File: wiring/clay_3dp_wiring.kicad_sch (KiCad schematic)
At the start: 1 part, among them J2 R3.CS

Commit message: update, but need to check references on hierchial sheets
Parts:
- removed J2: R3.CS, symbol Connector_Generic:Conn_01x12
- added A1: Arduino_UNO_R3, Module:Arduino_UNO_R3, symbol MCU_Module:Arduino_UNO_R3
- added J7, J8: TrimTrio connector on project box, symbol Connector_Generic:Conn_01x08
- added J9: 8P8C, symbol Connector:8P8C
- added M1: Stepper_Motor_bipolar, symbol Motor:Stepper_Motor_bipolar
- added U1: MotionKing_2L415B, symbol clay_3dp_wiring:MotionKing_2L415B
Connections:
- new net: J8.1 (Pin_1), M1.1, U1.7 (A+)
- new net: J8.2 (Pin_2), M1.2 (-), U1.8 (A-)
- new net: J8.4 (Pin_4), M1.3, U1.9 (B+)
- new net: J8.5 (Pin_5), M1.4, U1.10 (B-)
- new net 24V_plc_integration_shield/24V IN ORANGE: J7.1 (Pin_1)
- new net 24V_plc_integration_shield/Arduino D2: A1.17 (D2)
- new net 24V_plc_integration_shield/Arduino D4: A1.19 (D4)
- new net 24V_plc_integration_shield/Arduino D7: A1.22 (D7)
- new net 24V_plc_integration_shield/Arduino D8: A1.23 (D8)
- new net 24V_plc_integration_shield/Arduino D9: A1.24 (D9)
- new net 24V_plc_integration_shield/Arduino GND: A1.29 (GND), A1.6 (GND), A1.7 (GND)
- new net 24V_plc_integration_shield/Arduino VIN: A1.8 (VIN)
- new net 24V_plc_integration_shield/Direction signal BLUE: J7.6 (Pin_6)
- new net 24V_plc_integration_shield/GND IN BLACK: J7.3 (Pin_3)
- new net 24V_plc_integration_shield/Motor driver 24V GREY: U1.6 (+V)
- new net 24V_plc_integration_shield/Motor driver 5V PURPLE: U1.3 (OPTO)
- new net 24V_plc_integration_shield/Motor driver DIR WHITE: U1.2 (DIR)
- new net 24V_plc_integration_shield/Motor driver GND YELLOW: U1.5 (GND)
- new net 24V_plc_integration_shield/Motor driver PUL GREEN: U1.1 (PUL)
- new net 24V_plc_integration_shield/Motor driver ~{ENABLE} BROWN: U1.4 (~{ENABLE})
- new net 24V_plc_integration_shield/Run signal RED: J7.5 (Pin_5)
- no-connect marks 0 -> 41
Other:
- added sheet 24V_plc_integration_shield (C:/Users/tetov/src/extruder_ctrl_circuits/24V_plc_integration_shield/24V_plc_integration_shield.kicad_sch)
- added sheet lth2400_robban_io_wiring (lth2400_robban_io_wiring/lth2400_robban_io_wiring.kicad_sch)
- note added: "A+ GREEN (to TrimTrio) GREEN (between 8P8C and stepper)"
- note added: "A- BLACK (to TrimTrio) BLACK (between 8P8C and stepper)"
- note added: "B+ BROWN (to TrimTrio) RED (between 8P8C and stepper)"
- note added: "B- ? (to TrimTrio) ? (between 8P8C and stepper)"
- note added: "Motor driver"
- note added: "TODO: Check which poles on 8P8C are used"

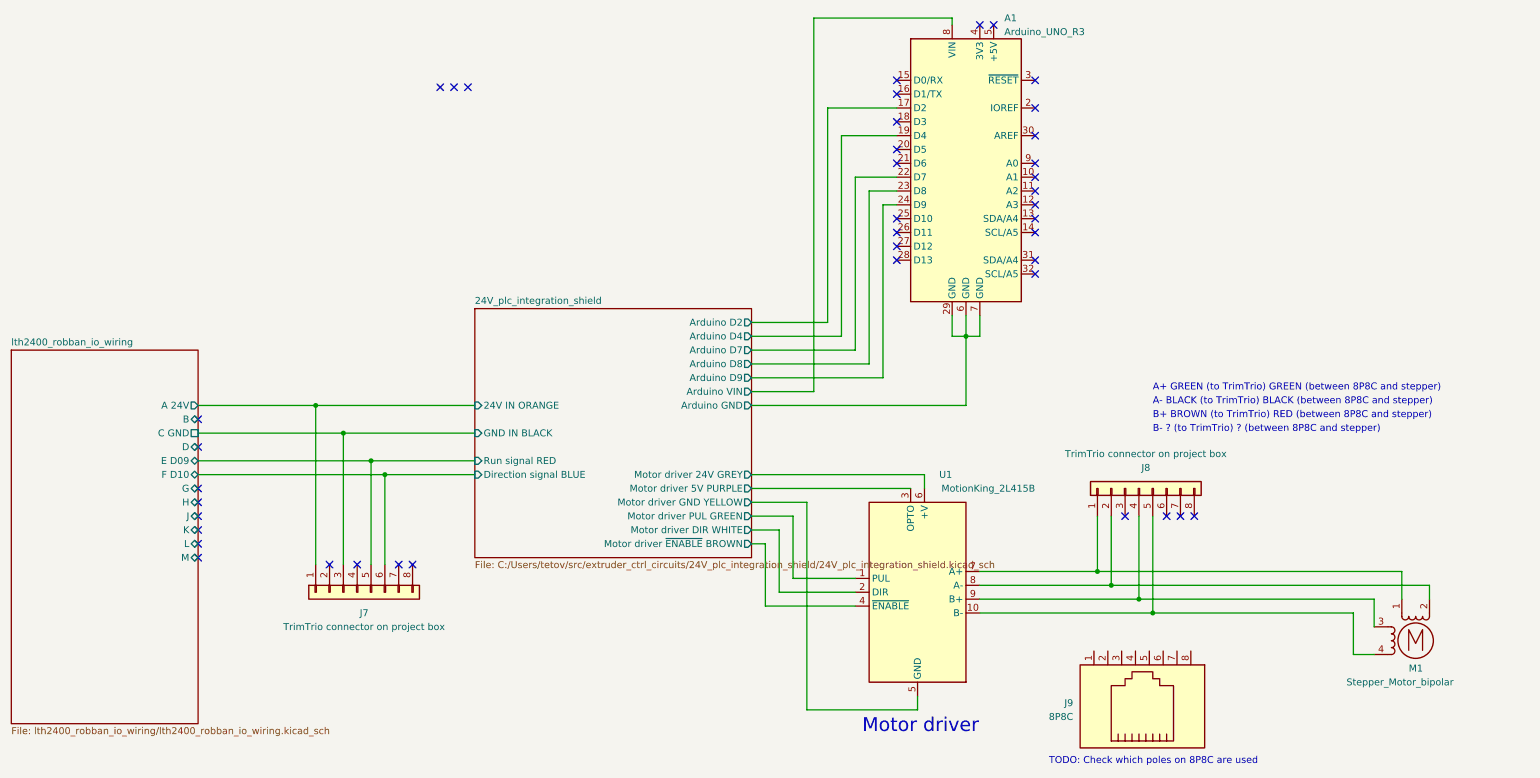
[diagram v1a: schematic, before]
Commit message: documentation of connectors and cable colors
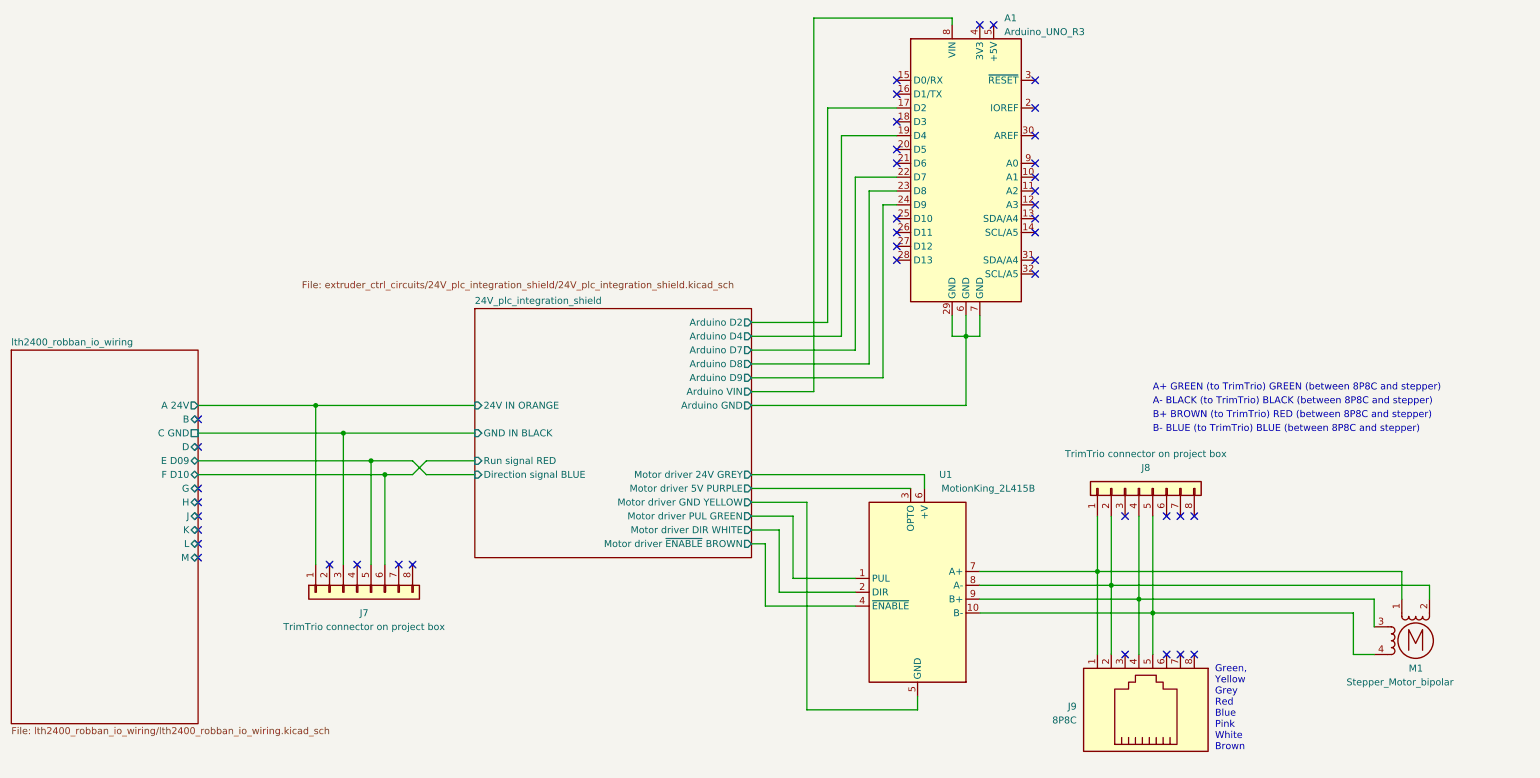
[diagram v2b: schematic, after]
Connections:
- net 24V_plc_integration_shield/Direction signal BLUE: now also J7.5 (Pin_5); no longer J7.6 (Pin_6)
- net 24V_plc_integration_shield/Run signal RED: now also J7.6 (Pin_6); no longer J7.5 (Pin_5)
- net at J9.1: now also J8.1 (Pin_1), M1.1, U1.7 (A+)
- net at J9.2: now also J8.2 (Pin_2), M1.2 (-), U1.8 (A-)
- net at J9.4: now also J8.4 (Pin_4), M1.3, U1.9 (B+)
- net at J9.5: now also J8.5 (Pin_5), M1.4, U1.10 (B-)
- no-connect marks 41 -> 42
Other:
- sheet 24V_plc_integration_shield: file C:/Users/tetov/src/extruder_ctrl_circuits/24V_plc_integration_shield/24V_plc_integration_shield.kicad_sch -> extruder_ctrl_circuits/24V_plc_integration_shield/24V_plc_integration_shield.kicad_sch
- note added: "B- BLUE (to TrimTrio) BLUE (between 8P8C and stepper)"
- note added: "Green, Yellow Grey Red Blue Pink White Brown"
- note removed: "B- ? (to TrimTrio) ? (between 8P8C and stepper)"
- note removed: "Motor driver"
- note removed: "TODO: Check which poles on 8P8C are used"
- moved on the sheet: J9
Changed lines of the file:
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@@
   (junction (at 217.17 118.11) (diameter 0) (color 0 0 0 0)
   )
+  (no_connect (at 232.41 130.81))
   (no_connect (at 193.04 15.24))
   (no_connect (at 49.53 100.33))
+  (no_connect (at 227.33 130.81))
   (no_connect (at 203.2 53.34))
   (no_connect (at 49.53 102.87))
@@
   (no_connect (at 49.53 110.49))
   (no_connect (at 177.8 55.88))
-  (no_connect (at 96.52 26.67))
   (no_connect (at 177.8 58.42))
   (no_connect (at 49.53 107.95))
@@
   (no_connect (at 232.41 105.41))
   (no_connect (at 49.53 87.63))
-  (no_connect (at 99.06 26.67))
   (no_connect (at 203.2 30.48))
   (no_connect (at 203.2 50.8))
   (no_connect (at 203.2 48.26))
   (no_connect (at 177.8 50.8))
+  (no_connect (at 219.71 130.81))
   (no_connect (at 229.87 105.41))
   (no_connect (at 203.2 40.64))
@@
   (no_connect (at 177.8 38.1))
   (no_connect (at 203.2 60.96))
-  (no_connect (at 93.98 26.67))
+  (no_connect (at 229.87 130.81))
   (wire (pts (xy 170.18 74.93) (xy 170.18 43.18))
     (stroke (width 0) (type default))
   )
+  (wire (pts (xy 88.9 95.25) (xy 91.44 97.79))
+    (stroke (width 0) (type default))
+  )
   (wire (pts (xy 275.59 120.65) (xy 275.59 118.11))
     (stroke (width 0) (type default))
@@
     (stroke (width 0) (type default))
   )
+  (wire (pts (xy 222.25 120.65) (xy 222.25 130.81))
+    (stroke (width 0) (type default))
+  )
   (wire (pts (xy 172.72 45.72) (xy 177.8 45.72))
     (stroke (width 0) (type default))
@@
     (stroke (width 0) (type default))
   )
+  (wire (pts (xy 88.9 97.79) (xy 91.44 95.25))
+    (stroke (width 0) (type default))
+  )
   (wire (pts (xy 49.53 95.25) (xy 81.28 95.25))
     (stroke (width 0) (type default))
   )
-  (wire (pts (xy 83.82 97.79) (xy 100.33 97.79))
+  (wire (pts (xy 83.82 97.79) (xy 88.9 97.79))
     (stroke (width 0) (type default))
   )
@@
     (stroke (width 0) (type default))
   )
+  (wire (pts (xy 214.63 115.57) (xy 214.63 130.81))
+    (stroke (width 0) (type default))
+  )
   (wire (pts (xy 76.2 90.17) (xy 100.33 90.17))
     (stroke (width 0) (type default))
@@
     (stroke (width 0) (type default))
   )
-  (wire (pts (xy 81.28 95.25) (xy 100.33 95.25))
+  (wire (pts (xy 81.28 95.25) (xy 88.9 95.25))
     (stroke (width 0) (type default))
   )
@@
     (stroke (width 0) (type default))
   )
+  (wire (pts (xy 91.44 97.79) (xy 100.33 97.79))
+    (stroke (width 0) (type default))
+  )
+  (wire (pts (xy 217.17 118.11) (xy 217.17 130.81))
+    (stroke (width 0) (type default))
+  )
   (wire (pts (xy 151.13 77.47) (xy 172.72 77.47))
     (stroke (width 0) (type default))
@@
     (stroke (width 0) (type default))
   )
+  (wire (pts (xy 91.44 95.25) (xy 100.33 95.25))
+    (stroke (width 0) (type default))
+  )
   (wire (pts (xy 158.75 105.41) (xy 158.75 116.84))
     (stroke (width 0) (type default))
@@
   )
   (wire (pts (xy 71.12 85.09) (xy 100.33 85.09))
+    (stroke (width 0) (type default))
+  )
+  (wire (pts (xy 224.79 123.19) (xy 224.79 130.81))
     (stroke (width 0) (type default))
   )
@@
     (effects (font (size 1.27 1.27)) (justify left bottom))
   )
-  (text "TODO: Check which poles on 8P8C are used" (at 205.74 151.13 0)
-    (effects (font (size 1.27 1.27)) (justify left bottom))
-  )
   (text "B+ BROWN (to TrimTrio) RED (between 8P8C and stepper)"
     (at 224.79 87.63 0)
     (effects (font (size 1.27 1.27)) (justify left bottom))
   )
-  (text "Motor driver" (at 171.45 145.415 0)
-    (effects (font (size 2.54 2.54)) (justify left bottom))
-  )
-  (text "B- ? (to TrimTrio) ? (between 8P8C and stepper)" (at 224.79 90.17 0)
+  (text "B- BLUE (to TrimTrio) BLUE (between 8P8C and stepper)"
+    (at 224.79 90.17 0)
+    (effects (font (size 1.27 1.27)) (justify left bottom))
+  )
+  (text "Green, \nYellow\nGrey\nRed\nBlue\nPink\nWhite\nBrown" (at 236.22 148.59 0)
     (effects (font (size 1.27 1.27)) (justify left bottom))
   )
@@
     (effects (font (size 1.27 1.27)) (justify left bottom))
   )
-  (symbol (lib_id "Connector:8P8C") (at 221.615 140.335 270) (mirror x) (unit 1)
+  (symbol (lib_id "Connector:8P8C") (at 222.25 140.97 270) (mirror x) (unit 1)
     (in_bom yes) (on_board yes) (dnp no)
-    (property "Reference" "J9" (at 210.185 139.7 90)
+    (property "Reference" "J9" (at 210.82 140.335 90)
       (effects (font (size 1.27 1.27)) (justify right))
     )
-    (property "Value" "8P8C" (at 210.185 142.24 90)
+    (property "Value" "8P8C" (at 210.82 142.875 90)
       (effects (font (size 1.27 1.27)) (justify right))
     )
-    (property "Footprint" "" (at 222.25 140.335 90)
-      (effects (font (size 1.27 1.27)) hide)
-    )
-    (property "Datasheet" "~" (at 222.25 140.335 90)
+    (property "Footprint" "" (at 222.885 140.97 90)
+      (effects (font (size 1.27 1.27)) hide)
+    )
+    (property "Datasheet" "~" (at 222.885 140.97 90)
       (effects (font (size 1.27 1.27)) hide)
     )
@@
     )
   )
-  (sheet (at 100.33 67.31) (size 50.8 45.72) (fields_autoplaced)
+  (sheet (at 100.33 67.31) (size 50.8 45.72)
     (stroke (width 0.1524) (type solid))
     (fill (color 0 0 0 0.0000))
@@
       (effects (font (size 1.27 1.27)) (justify left bottom))
     )
-    (property "Sheetfile" "C:/Users/tetov/src/extruder_ctrl_circuits/24V_plc_integration_shield/24V_plc_integration_shield.kicad_sch" (at 100.33 113.6146 0)
+    (property "Sheetfile" "extruder_ctrl_circuits/24V_plc_integration_shield/24V_plc_integration_shield.kicad_sch" (at 68.58 62.23 0)
       (effects (font (size 1.27 1.27)) (justify left top))
     )

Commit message: schematic text variables and symbol for RPi USB-C power
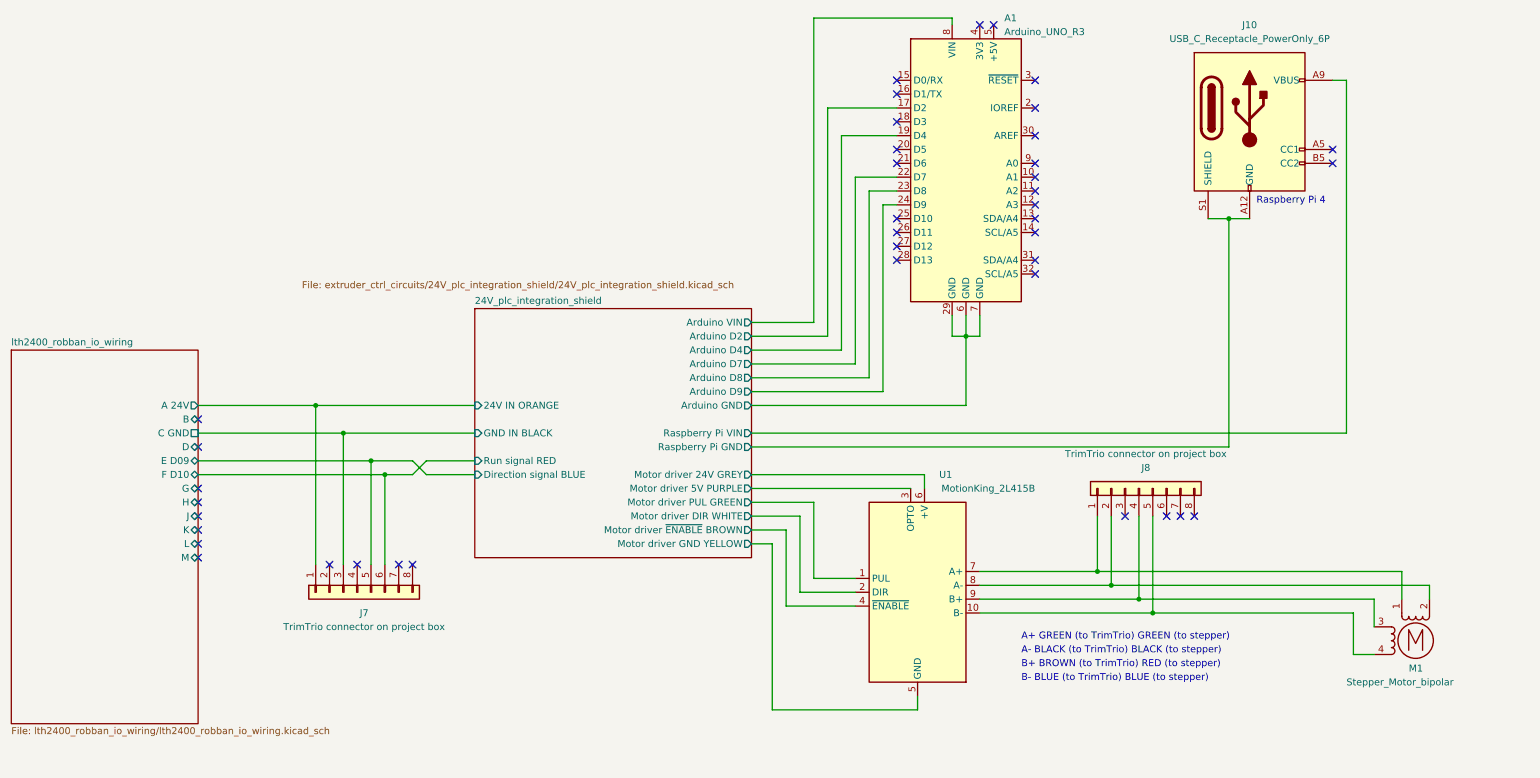
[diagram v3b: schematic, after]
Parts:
- removed J9: 8P8C, symbol Connector:8P8C
- added J10: USB_C_Receptacle_PowerOnly_6P, symbol Connector:USB_C_Receptacle_PowerOnly_6P
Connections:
- new net 24V_plc_integration_shield/Raspberry Pi GND: J10.A12 (GND), J10.B12 (GND), J10.S1 (SHIELD)
- new net 24V_plc_integration_shield/Raspberry Pi VIN: J10.A9 (VBUS), J10.B9 (VBUS)
- no-connect marks 42 -> 40
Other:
- sheet 24V_plc_integration_shield ports: added Raspberry Pi GND, Raspberry Pi VIN; removed none
- note added: "A+ GREEN (to TrimTrio) GREEN (to stepper)"
- note added: "A- BLACK (to TrimTrio) BLACK (to stepper)"
- note added: "B+ BROWN (to TrimTrio) RED (to stepper)"
- note added: "B- BLUE (to TrimTrio) BLUE (to stepper)"
- note added: "Raspberry Pi 4"
- note removed: "A+ GREEN (to TrimTrio) GREEN (between 8P8C and stepper)"
- note removed: "A- BLACK (to TrimTrio) BLACK (between 8P8C and stepper)"
- note removed: "B+ BROWN (to TrimTrio) RED (between 8P8C and stepper)"
- note removed: "B- BLUE (to TrimTrio) BLUE (between 8P8C and stepper)"
- note removed: "Green, Yellow Grey Red Blue Pink White Brown"
- company: (none) -> ${company}
- title: (none) -> ${project_title}

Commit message: move stepper driver to irc5 cabinet
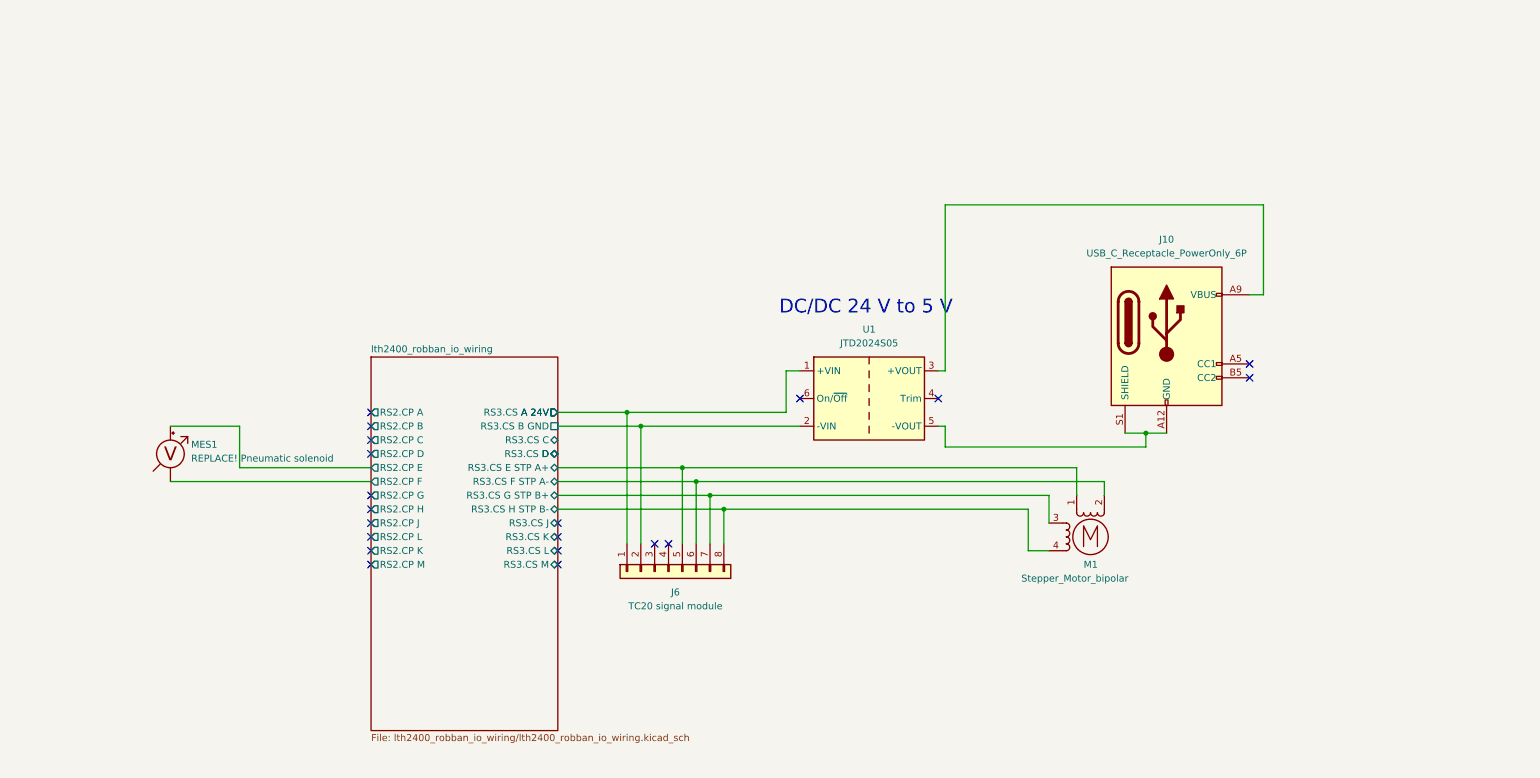
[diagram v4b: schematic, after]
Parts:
- removed A1: Arduino_UNO_R3, Module:Arduino_UNO_R3, symbol MCU_Module:Arduino_UNO_R3
- removed J7, J8: TrimTrio connector on project box, symbol Connector_Generic:Conn_01x08
- removed U1: MotionKing_2L415B, symbol clay_3dp_wiring:MotionKing_2L415B
- added J6: TC20 signal module, symbol Connector_Generic:Conn_01x08
- added MES1: REPLACE! Pneumatic solenoid, symbol Device:Voltmeter_DC
- added U1: JTD2024S05, Converter_DCDC:Converter_DCDC_XP_POWER_JTDxxxxxxx_THT, symbol Converter_DCDC:JTD2024S05
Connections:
- net lth2400_robban_io_wiring/RS3.CS E STP A+: now reaches M1.1
- net lth2400_robban_io_wiring/RS3.CS E STP A+: now also J6.5 (Pin_5)
- net lth2400_robban_io_wiring/RS3.CS F STP A-: now reaches M1.2 (-)
- net lth2400_robban_io_wiring/RS3.CS F STP A-: now also J6.6 (Pin_6)
- net lth2400_robban_io_wiring/RS3.CS G STP B+: now reaches M1.3
- net lth2400_robban_io_wiring/RS3.CS G STP B+: now also J6.7 (Pin_7)
- net lth2400_robban_io_wiring/RS3.CS H STP B-: now reaches M1.4
- net lth2400_robban_io_wiring/RS3.CS H STP B-: now also J6.8 (Pin_8)
- net 24V_plc_integration_shield/Raspberry Pi GND: no longer names the net of J10.A12 (GND), J10.B12 (GND), J10.S1 (SHIELD)
- net 24V_plc_integration_shield/Raspberry Pi GND: now also U1.5 (-VOUT)
- net 24V_plc_integration_shield/Raspberry Pi VIN: no longer names the net of J10.A9 (VBUS), J10.B9 (VBUS)
- net 24V_plc_integration_shield/Raspberry Pi VIN: now also U1.3 (+VOUT)
- new net lth2400_robban_io_wiring/A 24V: J6.1 (Pin_1), U1.1 (+VIN)
- new net lth2400_robban_io_wiring/RS2.CP E: MES1.2 (+)
- new net lth2400_robban_io_wiring/RS2.CP F: MES1.1 (-)
- new net lth2400_robban_io_wiring/RS3.CS B GND: J6.2 (Pin_2), U1.2 (-VIN)
- no-connect marks 40 -> 20
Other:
- removed sheet 24V_plc_integration_shield
- sheet lth2400_robban_io_wiring ports: added RS2.CP A, RS2.CP B, RS2.CP C, RS2.CP D, RS2.CP E, RS2.CP F, RS2.CP G, RS2.CP H, RS2.CP J, RS2.CP K, RS2.CP L, RS2.CP M, RS3.CS A 24V, RS3.CS B GND, RS3.CS C, RS3.CS D, RS3.CS E STP A+, RS3.CS F STP A-, RS3.CS G STP B+, RS3.CS H STP B-, RS3.CS J, RS3.CS K, RS3.CS L, RS3.CS M; removed B, C GND, E D09, F D10, G, H, J, K, L, M
- note added: "DC/DC 24 V to 5 V"
- note removed: "A+ GREEN (to TrimTrio) GREEN (to stepper)"
- note removed: "A- BLACK (to TrimTrio) BLACK (to stepper)"
- note removed: "B+ BROWN (to TrimTrio) RED (to stepper)"
- note removed: "B- BLUE (to TrimTrio) BLUE (to stepper)"
- note removed: "Raspberry Pi 4"
- moved on the sheet: J10, M1
